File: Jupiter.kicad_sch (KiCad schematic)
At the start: 347 parts, among them SW1 SW_Push, U1 ATmega32U4-M, Y1 Crystal_GND24_Small

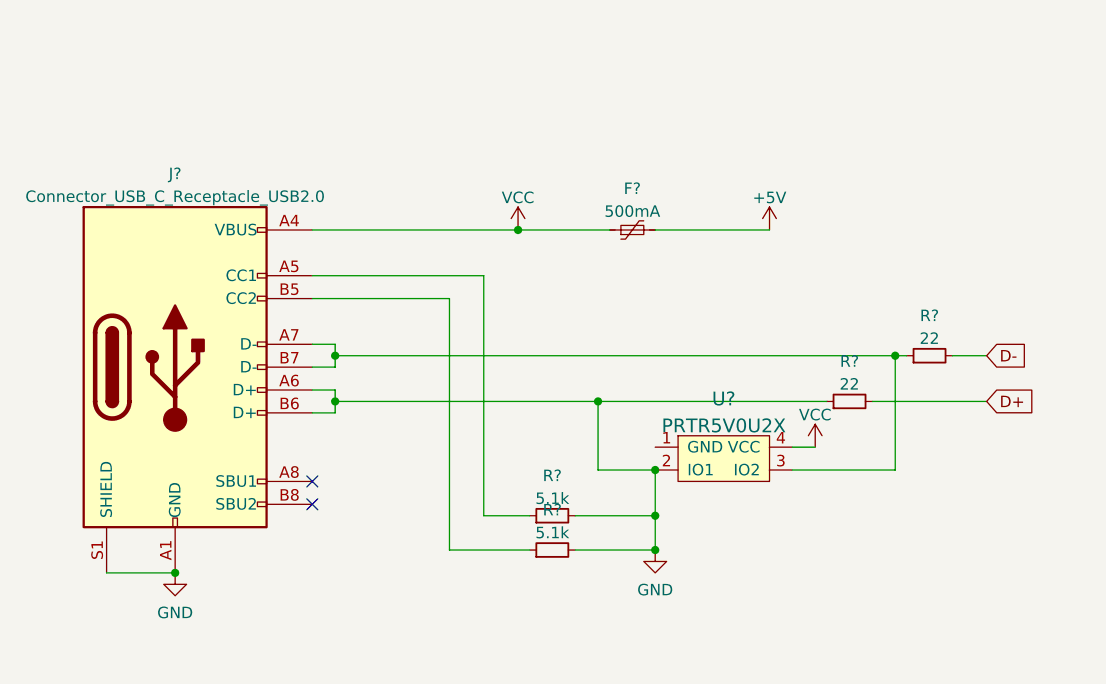
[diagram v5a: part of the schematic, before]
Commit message: Finished usb-c assembly
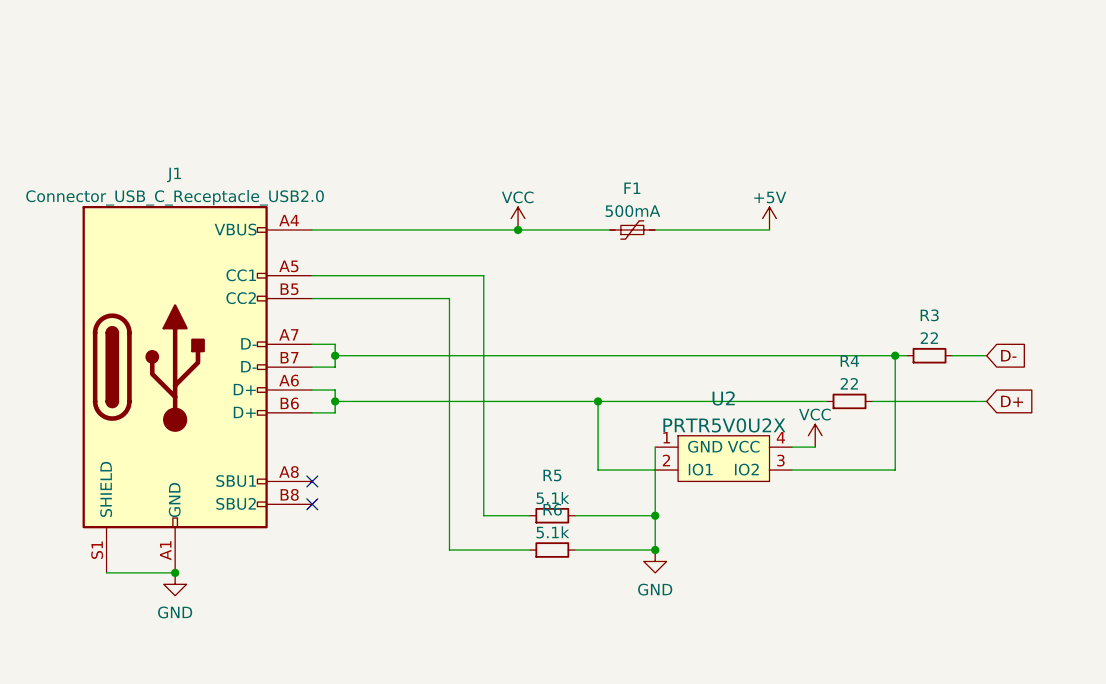
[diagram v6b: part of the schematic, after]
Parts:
- F1: renamed from F?; footprint (none) -> Fuse:Fuse_1206_3216Metric
- J1: renamed from J?; footprint (none) -> marbastlib-various:USB_C_Receptacle_HRO_TYPE-C-31-M-14
- R3, R4, R5, R6: renamed from R?; footprint (none) -> Resistor_SMD:R_0603_1608Metric
- U2: renamed from U?; footprint (none) -> random-keyboard-parts:SOT143B
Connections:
- net GND: now also U2.1 (GND); no longer J1.A6 (D+), J1.B6 (D+), R4.1, U2.2 (IO1)
- new net: J1.A6 (D+), J1.B6 (D+), R4.1, U2.2 (IO1)
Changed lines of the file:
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@@
   (junction (at 90.17 114.3) (diameter 0) (color 0 0 0 0)
   )
-  (junction (at 519.43 69.85) (diameter 0) (color 0 0 0 0)
-  )
   (junction (at 140.97 351.79) (diameter 0) (color 0 0 0 0)
   )
@@
   (junction (at 252.73 198.12) (diameter 0) (color 0 0 0 0)
   )
+  (junction (at 519.43 69.85) (diameter 0) (color 0 0 0 0)
+  )
   (junction (at 100.33 152.4) (diameter 0) (color 0 0 0 0)
   )
@@
   (junction (at 292.1 386.08) (diameter 0) (color 0 0 0 0)
   )
-  (junction (at 519.43 64.77) (diameter 0) (color 0 0 0 0)
-  )
   (junction (at 292.1 363.22) (diameter 0) (color 0 0 0 0)
   )
@@
     (stroke (width 0) (type default) (color 0 0 0 0))
   )
+  (wire (pts (xy 519.43 62.23) (xy 519.43 69.85))
+    (stroke (width 0) (type default) (color 0 0 0 0))
+  )
   (wire (pts (xy 313.69 242.57) (xy 344.17 242.57))
     (stroke (width 0) (type default) (color 0 0 0 0))
@@
     (stroke (width 0) (type default) (color 0 0 0 0))
   )
-  (wire (pts (xy 519.43 64.77) (xy 519.43 69.85))
-    (stroke (width 0) (type default) (color 0 0 0 0))
-  )
   (wire (pts (xy 223.52 95.25) (xy 240.03 95.25))
     (stroke (width 0) (type default) (color 0 0 0 0))
@@
   (symbol (lib_id "power:GND") (at 466.09 76.2 0) (unit 1)
     (in_bom yes) (on_board yes) (fields_autoplaced)
-    (property "Reference" "#PWR?" (id 0) (at 466.09 82.55 0)
+    (property "Reference" "#PWR0109" (id 0) (at 466.09 82.55 0)
       (effects (font (size 1.27 1.27)) hide)
     )
@@
   (symbol (lib_id "power:+5V") (at 532.13 38.1 0) (unit 1)
     (in_bom yes) (on_board yes) (fields_autoplaced)
-    (property "Reference" "#PWR?" (id 0) (at 532.13 41.91 0)
+    (property "Reference" "#PWR0110" (id 0) (at 532.13 41.91 0)
       (effects (font (size 1.27 1.27)) hide)
     )
@@
   (symbol (lib_id "power:VCC") (at 504.19 38.1 0) (unit 1)
     (in_bom yes) (on_board yes) (fields_autoplaced)
-    (property "Reference" "#PWR?" (id 0) (at 504.19 41.91 0)
+    (property "Reference" "#PWR0118" (id 0) (at 504.19 41.91 0)
       (effects (font (size 1.27 1.27)) hide)
     )
@@
   (symbol (lib_id "USB-C-USB-2.0-cache:Connector_USB_C_Receptacle_USB2.0") (at 466.09 53.34 0) (unit 1)
     (in_bom yes) (on_board yes) (fields_autoplaced)
-    (property "Reference" "J?" (id 0) (at 466.09 31.8602 0))
+    (property "Reference" "J1" (id 0) (at 466.09 31.8602 0))
     (property "Value" "Connector_USB_C_Receptacle_USB2.0" (id 1) (at 466.09 34.3971 0))
-    (property "Footprint" "" (id 2) (at 469.9 53.34 0)
+    (property "Footprint" "marbastlib-various:USB_C_Receptacle_HRO_TYPE-C-31-M-14" (id 2) (at 469.9 53.34 0)
       (effects (font (size 1.27 1.27)) hide)
     )
@@
   (symbol (lib_id "random-keyboard-parts:PRTR5V0U2X") (at 527.05 63.5 0) (unit 1)
     (in_bom yes) (on_board yes) (fields_autoplaced)
-    (property "Reference" "U?" (id 0) (at 527.05 56.8759 0)
+    (property "Reference" "U2" (id 0) (at 527.05 56.8759 0)
       (effects (font (size 1.524 1.524)))
     )
@@
       (effects (font (size 1.524 1.524)))
     )
-    (property "Footprint" "" (id 2) (at 527.05 63.5 0)
+    (property "Footprint" "random-keyboard-parts:SOT143B" (id 2) (at 527.05 63.5 0)
       (effects (font (size 1.524 1.524)) hide)
     )
@@
   (symbol (lib_id "power:VCC") (at 537.21 62.23 0) (unit 1)
     (in_bom yes) (on_board yes) (fields_autoplaced)
-    (property "Reference" "#PWR?" (id 0) (at 537.21 66.04 0)
+    (property "Reference" "#PWR0117" (id 0) (at 537.21 66.04 0)
       (effects (font (size 1.27 1.27)) hide)
     )
@@
   (symbol (lib_id "Device:R_Small") (at 508 69.85 90) (unit 1)
     (in_bom yes) (on_board yes) (fields_autoplaced)
-    (property "Reference" "R?" (id 0) (at 508 65.4136 90))
+    (property "Reference" "R5" (id 0) (at 508 65.4136 90))
     (property "Value" "5.1k" (id 1) (at 508 67.9505 90))
-    (property "Footprint" "" (id 2) (at 508 69.85 0)
+    (property "Footprint" "Resistor_SMD:R_0603_1608Metric" (id 2) (at 508 69.85 0)
       (effects (font (size 1.27 1.27)) hide)
     )
@@
   (symbol (lib_id "Device:R_Small") (at 508 73.66 90) (unit 1)
     (in_bom yes) (on_board yes) (fields_autoplaced)
-    (property "Reference" "R?" (id 0) (at 508 69.2236 90))
+    (property "Reference" "R6" (id 0) (at 508 69.2236 90))
     (property "Value" "5.1k" (id 1) (at 508 71.7605 90))
-    (property "Footprint" "" (id 2) (at 508 73.66 0)
+    (property "Footprint" "Resistor_SMD:R_0603_1608Metric" (id 2) (at 508 73.66 0)
       (effects (font (size 1.27 1.27)) hide)
     )
@@
   (symbol (lib_id "Device:R_Small") (at 541.02 57.15 90) (unit 1)
     (in_bom yes) (on_board yes) (fields_autoplaced)
-    (property "Reference" "R?" (id 0) (at 541.02 52.7136 90))
+    (property "Reference" "R4" (id 0) (at 541.02 52.7136 90))
     (property "Value" "22" (id 1) (at 541.02 55.2505 90))
-    (property "Footprint" "" (id 2) (at 541.02 57.15 0)
+    (property "Footprint" "Resistor_SMD:R_0603_1608Metric" (id 2) (at 541.02 57.15 0)
       (effects (font (size 1.27 1.27)) hide)
     )
@@
   (symbol (lib_id "Device:Polyfuse_Small") (at 516.89 38.1 90) (unit 1)
     (in_bom yes) (on_board yes) (fields_autoplaced)
-    (property "Reference" "F?" (id 0) (at 516.89 33.5112 90))
+    (property "Reference" "F1" (id 0) (at 516.89 33.5112 90))
     (property "Value" "500mA" (id 1) (at 516.89 36.0481 90))
-    (property "Footprint" "" (id 2) (at 521.97 36.83 0)
+    (property "Footprint" "Fuse:Fuse_1206_3216Metric" (id 2) (at 521.97 36.83 0)
       (effects (font (size 1.27 1.27)) (justify left) hide)
     )
@@
   (symbol (lib_id "Device:R_Small") (at 549.91 52.07 90) (unit 1)
     (in_bom yes) (on_board yes) (fields_autoplaced)
-    (property "Reference" "R?" (id 0) (at 549.91 47.6336 90))
+    (property "Reference" "R3" (id 0) (at 549.91 47.6336 90))
     (property "Value" "22" (id 1) (at 549.91 50.1705 90))
-    (property "Footprint" "" (id 2) (at 549.91 52.07 0)
+    (property "Footprint" "Resistor_SMD:R_0603_1608Metric" (id 2) (at 549.91 52.07 0)
       (effects (font (size 1.27 1.27)) hide)
     )
@@
   (symbol (lib_id "power:GND") (at 519.43 73.66 0) (unit 1)
     (in_bom yes) (on_board yes) (fields_autoplaced)
-    (property "Reference" "#PWR?" (id 0) (at 519.43 80.01 0)
+    (property "Reference" "#PWR0119" (id 0) (at 519.43 80.01 0)
       (effects (font (size 1.27 1.27)) hide)
     )
@@
       (reference "#PWR0108") (unit 1) (value "+5V") (footprint "")
     )
+    (path "/1a853bec-a5b0-4182-9ebb-c3db3d497370"
+      (reference "#PWR0109") (unit 1) (value "GND") (footprint "")
+    )
+    (path "/29f4c1eb-6384-43cf-a1dc-29fc79670556"
+      (reference "#PWR0110") (unit 1) (value "+5V") (footprint "")
+    )
     (path "/3343379b-1d26-41c6-8015-955e176890b7"
       (reference "#PWR0111") (unit 1) (value "GND") (footprint "")
@@
       (reference "#PWR0116") (unit 1) (value "GND") (footprint "")
     )
-    (path "/1a853bec-a5b0-4182-9ebb-c3db3d497370"
-      (reference "#PWR?") (unit 1) (value "GND") (footprint "")
-    )
-    (path "/29f4c1eb-6384-43cf-a1dc-29fc79670556"
-      (reference "#PWR?") (unit 1) (value "+5V") (footprint "")
+    (path "/7e537112-97b3-461a-9476-143d1b62889d"
+      (reference "#PWR0117") (unit 1) (value "VCC") (footprint "")
     )
     (path "/420034f2-5c0b-42e1-bffd-0fdb40e4bbe6"
-      (reference "#PWR?") (unit 1) (value "VCC") (footprint "")
-    )
-    (path "/7e537112-97b3-461a-9476-143d1b62889d"
-      (reference "#PWR?") (unit 1) (value "VCC") (footprint "")
+      (reference "#PWR0118") (unit 1) (value "VCC") (footprint "")
     )
     (path "/fe6eeca3-df26-4a38-ad33-9eb31c26b9b9"
-      (reference "#PWR?") (unit 1) (value "GND") (footprint "")
+      (reference "#PWR0119") (unit 1) (value "GND") (footprint "")
     )
     (path "/213d1ae6-3493-4a17-9c56-b781ec3d5fab"
@@
     )
     (path "/c16d0013-4ad3-4974-b494-e8139c1e7f2b"
-      (reference "F?") (unit 1) (value "500mA") (footprint "")
+      (reference "F1") (unit 1) (value "500mA") (footprint "Fuse:Fuse_1206_3216Metric")
     )
     (path "/59ae39a2-cb9c-4d24-8c9e-792b7b0ffd9c"
-      (reference "J?") (unit 1) (value "Connector_USB_C_Receptacle_USB2.0") (footprint "")
+      (reference "J1") (unit 1) (value "Connector_USB_C_Receptacle_USB2.0") (footprint "marbastlib-various:USB_C_Receptacle_HRO_TYPE-C-31-M-14")
     )
     (path "/9de686b4-dca8-4f88-a6cb-b8703cee154a"
@@
       (reference "R2") (unit 1) (value "1k") (footprint "Resistor_SMD:R_0603_1608Metric")
     )
-    (path "/a262535b-6894-4840-8bc5-64fe50cf0d6a"
-      (reference "R?") (unit 1) (value "5.1k") (footprint "")
-    )
-    (path "/b245d22d-2850-402a-ad41-44b03576cca4"
-      (reference "R?") (unit 1) (value "5.1k") (footprint "")
+    (path "/f6530bbb-3235-446b-90bd-62bba5916f8f"
+      (reference "R3") (unit 1) (value "22") (footprint "Resistor_SMD:R_0603_1608Metric")
     )
     (path "/c0d15e4a-ba5d-4176-87b9-5561f2edf504"
-      (reference "R?") (unit 1) (value "22") (footprint "")
+      (reference "R4") (unit 1) (value "22") (footprint "Resistor_SMD:R_0603_1608Metric")
     )
-    (path "/f6530bbb-3235-446b-90bd-62bba5916f8f"
-      (reference "R?") (unit 1) (value "22") (footprint "")
+    (path "/a262535b-6894-4840-8bc5-64fe50cf0d6a"
+      (reference "R5") (unit 1) (value "5.1k") (footprint "Resistor_SMD:R_0603_1608Metric")
+    )
+    (path "/b245d22d-2850-402a-ad41-44b03576cca4"
+      (reference "R6") (unit 1) (value "5.1k") (footprint "Resistor_SMD:R_0603_1608Metric")
     )
     (path "/20226c85-96ea-44d3-a255-4e1300fb3be7"
@@
     )
     (path "/5e25d345-8130-4e41-bd8d-fd468aef5828"
-      (reference "U?") (unit 1) (value "PRTR5V0U2X") (footprint "")
+      (reference "U2") (unit 1) (value "PRTR5V0U2X") (footprint "random-keyboard-parts:SOT143B")
     )
     (path "/1da16e64-cd89-47c6-a15d-a5d97941d7ac"

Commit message: Corrected LED orientation
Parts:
- LED_0, LED_1, LED_2, LED_3, LED_4, LED_5, LED_6, LED_7, LED_8, LED_9, LED_A1, LED_D1, LED_F13, LED_G1, LED_H1, LED_J1, LED_K1, LED_L1, LED_S1, LED_backspace1, LED_capsLock1, LED_colon1, LED_downArrow1, LED_end1, LED_enter1, LED_equals1, LED_function1, LED_leftAlt1, LED_leftArrow1, LED_leftControl1, LED_minus1, LED_pgDn1, LED_pgUp1, LED_quote1, LED_rightAlt1, LED_rightArrow1, LED_rightControl1, LED_space1, LED_tilda1, LED_windows1: footprint marbastlib-mx:LED_MX_6028R-FLIPPED -> marbastlib-mx:LED_MX_6028R
- LED_B1, LED_C1, LED_E1, LED_F1, LED_F10, LED_F11, LED_F12, LED_F2, LED_F3, LED_F4, LED_F5, LED_F6, LED_F7, LED_F8, LED_F9, LED_I1, LED_M1, LED_N1, LED_O1, LED_P1, LED_Q1, LED_R1, LED_T1, LED_U1, LED_V1, LED_W1, LED_X1, LED_Y1, LED_Z1, LED_backslash1, LED_closeBracket1, LED_comma1, LED_delete1, LED_esc1, LED_home1, LED_leftShift1, LED_openBracket1, LED_period1, LED_questionMark1, LED_rightShift1, LED_tab1, LED_upArrow1: footprint marbastlib-mx:LED_MX_6028R -> marbastlib-mx:LED_MX_6028R-FLIPPED
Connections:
- net COL14: now also U1.10 (PB2); no longer U1.9 (PB1)
- net GND: now also J1.A6 (D+), J1.B6 (D+), R4.1, U2.2 (IO1); no longer U2.1 (GND)
- net RGBLED: now also LED_home1.3 (DIN), U1.9 (PB1); no longer LED_end1.3 (DIN), U1.12 (PB7)
- net ROW4: now also U1.11 (PB3); no longer U1.10 (PB2)
- net ROW5: now also U1.12 (PB7); no longer U1.11 (PB3)
- net at LED_Q1.2 (DOUT): now also LED_W1.3 (DIN); no longer LED_tab1.3 (DIN)
- net at LED_Q1.3 (DIN): now also LED_tab1.2 (DOUT); no longer LED_W1.2 (DOUT)
- net at LED_upArrow1.2 (DOUT): now also LED_enter1.3 (DIN); no longer LED_rightShift1.3 (DIN)
- net at LED_upArrow1.3 (DIN): now also LED_rightShift1.2 (DOUT); no longer LED_enter1.2 (DOUT)
- net at LED_F2.2 (DOUT): now also LED_F3.3 (DIN); no longer LED_F1.3 (DIN)
- net at LED_F2.3 (DIN): now also LED_F1.2 (DOUT); no longer LED_F3.2 (DOUT)
- net at LED_leftControl1.2 (DOUT): now also LED_leftShift1.3 (DIN); no longer LED_windows1.3 (DIN)
- net at LED_leftControl1.3 (DIN): now also LED_windows1.2 (DOUT); no longer LED_leftShift1.2 (DOUT)
- net at LED_K1.2 (DOUT): now also LED_J1.3 (DIN); no longer LED_L1.3 (DIN)
- net at LED_K1.3 (DIN): now also LED_L1.2 (DOUT); no longer LED_J1.2 (DOUT)
- net at LED_leftArrow1.2 (DOUT): now also LED_rightControl1.3 (DIN); no longer LED_downArrow1.3 (DIN)
- net at LED_leftArrow1.3 (DIN): now also LED_downArrow1.2 (DOUT); no longer LED_rightControl1.2 (DOUT)
- net at LED_colon1.3 (DIN): now also LED_quote1.2 (DOUT); no longer LED_L1.2 (DOUT)
- net at LED_F6.2 (DOUT): now also LED_F7.3 (DIN); no longer LED_F5.3 (DIN)
- net at LED_F6.3 (DIN): now also LED_F5.2 (DOUT); no longer LED_F7.2 (DOUT)
- net at LED_questionMark1.2 (DOUT): now also LED_rightShift1.3 (DIN); no longer LED_period1.3 (DIN)
- net at LED_questionMark1.3 (DIN): now also LED_period1.2 (DOUT); no longer LED_rightShift1.2 (DOUT)
- net at LED_4.2 (DOUT): now also LED_3.3 (DIN); no longer LED_5.3 (DIN)
- net at LED_4.3 (DIN): now also LED_5.2 (DOUT); no longer LED_3.2 (DOUT)
- net at LED_Z1.2 (DOUT): now also LED_X1.3 (DIN); no longer LED_leftShift1.3 (DIN)
- net at LED_minus1.2 (DOUT): now also LED_0.3 (DIN); no longer LED_equals1.3 (DIN)
- net at LED_minus1.3 (DIN): now also LED_equals1.2 (DOUT); no longer LED_0.2 (DOUT)
- net at LED_leftAlt1.3 (DIN): now also LED_space1.2 (DOUT); no longer LED_windows1.2 (DOUT)
- net at LED_9.2 (DOUT): now also LED_8.3 (DIN); no longer LED_0.3 (DIN)
- net at LED_9.3 (DIN): now also LED_0.2 (DOUT); no longer LED_8.2 (DOUT)
- net at LED_S1.2 (DOUT): now also LED_A1.3 (DIN); no longer LED_D1.3 (DIN)
- net at LED_S1.3 (DIN): now also LED_D1.2 (DOUT); no longer LED_A1.2 (DOUT)
- net at LED_esc1.3 (DIN): now also LED_tilda1.2 (DOUT); no longer LED_F1.2 (DOUT)
- net at LED_rightArrow1.2 (DOUT): now also LED_downArrow1.3 (DIN)
- net at LED_rightArrow1.3 (DIN): now also LED_end1.2 (DOUT); no longer LED_downArrow1.2 (DOUT)
- net at LED_F8.2 (DOUT): now also LED_F9.3 (DIN); no longer LED_F7.3 (DIN)
- net at LED_F4.2 (DOUT): now also LED_F5.3 (DIN); no longer LED_F3.3 (DIN)
- net at LED_C1.2 (DOUT): now also LED_V1.3 (DIN); no longer LED_X1.3 (DIN)
- net at LED_C1.3 (DIN): now also LED_X1.2 (DOUT); no longer LED_V1.2 (DOUT)
- net at LED_backspace1.2 (DOUT): now also LED_equals1.3 (DIN); no longer LED_backslash1.3 (DIN)
- net at LED_backspace1.3 (DIN): now also LED_backslash1.2 (DOUT); no longer LED_equals1.2 (DOUT)
- net at LED_F4.3 (DIN): now also LED_F3.2 (DOUT); no longer LED_F5.2 (DOUT)
- net at LED_Y1.2 (DOUT): now also LED_U1.3 (DIN); no longer LED_T1.3 (DIN)
- net at LED_Y1.3 (DIN): now also LED_T1.2 (DOUT); no longer LED_U1.2 (DOUT)
- net at LED_function1.2 (DOUT): now also LED_rightAlt1.3 (DIN); no longer LED_rightControl1.3 (DIN)
- net at LED_function1.3 (DIN): now also LED_rightControl1.2 (DOUT); no longer LED_rightAlt1.2 (DOUT)
- net at LED_pgUp1.2 (DOUT): now also LED_pgDn1.3 (DIN); no longer LED_home1.3 (DIN)
- net at LED_pgUp1.3 (DIN): now also LED_home1.2 (DOUT); no longer LED_pgDn1.2 (DOUT)
- net at LED_M1.2 (DOUT): now also LED_comma1.3 (DIN); no longer LED_N1.3 (DIN)
- net at LED_M1.3 (DIN): now also LED_N1.2 (DOUT); no longer LED_comma1.2 (DOUT)
- net at LED_delete1.2 (DOUT): no longer LED_F12.3 (DIN)
- net at LED_delete1.3 (DIN): now also LED_F12.2 (DOUT); no longer LED_home1.2 (DOUT)
- net at LED_R1.2 (DOUT): now also LED_T1.3 (DIN); no longer LED_E1.3 (DIN)
- net at LED_R1.3 (DIN): now also LED_E1.2 (DOUT); no longer LED_T1.2 (DOUT)
- net at LED_Z1.3 (DIN): now also LED_leftShift1.2 (DOUT); no longer LED_X1.2 (DOUT)
- net at LED_F8.3 (DIN): now also LED_F7.2 (DOUT); no longer LED_F9.2 (DOUT)
- net at LED_2.2 (DOUT): now also LED_1.3 (DIN); no longer LED_3.3 (DIN)
- net at LED_2.3 (DIN): now also LED_3.2 (DOUT); no longer LED_1.2 (DOUT)
- net at LED_leftAlt1.2 (DOUT): now also LED_windows1.3 (DIN); no longer LED_space1.3 (DIN)
- net at LED_F11.2 (DOUT): now also LED_F12.3 (DIN); no longer LED_F10.3 (DIN)
- net at LED_F11.3 (DIN): now also LED_F10.2 (DOUT); no longer LED_F12.2 (DOUT)
- net at LED_colon1.2 (DOUT): now also LED_L1.3 (DIN); no longer LED_quote1.3 (DIN)
- net at LED_capsLock1.2 (DOUT): now also LED_tab1.3 (DIN); no longer LED_A1.3 (DIN)
- net at LED_7.2 (DOUT): now also LED_6.3 (DIN); no longer LED_8.3 (DIN)
- net at LED_7.3 (DIN): now also LED_8.2 (DOUT); no longer LED_6.2 (DOUT)
- net at LED_esc1.2 (DOUT): now also LED_F1.3 (DIN); no longer LED_tilda1.3 (DIN)
- net at LED_capsLock1.3 (DIN): now also LED_A1.2 (DOUT); no longer LED_tab1.2 (DOUT)
- net at LED_closeBracket1.3 (DIN): now also LED_openBracket1.2 (DOUT); no longer LED_backslash1.2 (DOUT)
- net at LED_B1.2 (DOUT): now also LED_N1.3 (DIN); no longer LED_V1.3 (DIN)
- net at LED_G1.2 (DOUT): now also LED_F13.3 (DIN); no longer LED_H1.3 (DIN)
- net at LED_G1.3 (DIN): now also LED_H1.2 (DOUT); no longer LED_F13.2 (DOUT)
- net at LED_closeBracket1.2 (DOUT): now also LED_backslash1.3 (DIN); no longer LED_openBracket1.3 (DIN)
- net at LED_B1.3 (DIN): now also LED_V1.2 (DOUT); no longer LED_N1.2 (DOUT)
- net at LED_P1.3 (DIN): now also LED_O1.2 (DOUT); no longer LED_openBracket1.2 (DOUT)
- net at LED_P1.2 (DOUT): now also LED_openBracket1.3 (DIN); no longer LED_O1.3 (DIN)
- net at LED_I1.2 (DOUT): now also LED_O1.3 (DIN); no longer LED_U1.3 (DIN)
- net at LED_I1.3 (DIN): now also LED_U1.2 (DOUT); no longer LED_O1.2 (DOUT)
- new net: LED_E1.3 (DIN), LED_W1.2 (DOUT)
- new net: LED_end1.3 (DIN), LED_pgDn1.2 (DOUT)
- new net: LED_comma1.2 (DOUT), LED_period1.3 (DIN)
- new net: LED_enter1.2 (DOUT), LED_quote1.3 (DIN)
- new net: LED_F10.3 (DIN), LED_F9.2 (DOUT)
- new net: LED_1.2 (DOUT), LED_tilda1.3 (DIN)
- new net: LED_5.3 (DIN), LED_6.2 (DOUT)
- new net: LED_rightAlt1.2 (DOUT), LED_space1.3 (DIN)
- new net: LED_D1.3 (DIN), LED_F13.2 (DOUT)
- new net: LED_H1.3 (DIN), LED_J1.2 (DOUT)
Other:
- moved on the sheet: C1, C10, C11, C12, C13, C14, C15, C16, C17, C18, C19, C2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

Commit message: Finished trace routing
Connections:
- net GND: now also U2.1 (GND); no longer J1.A6 (D+), J1.B6 (D+), R4.1, U2.2 (IO1)
- new net: J1.A6 (D+), J1.B6 (D+), R4.1, U2.2 (IO1)
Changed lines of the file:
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@@
   (junction (at 332.74 265.43) (diameter 0) (color 0 0 0 0)
-  )
-  (junction (at 317.5 381) (diameter 0) (color 0 0 0 0)
   )
   (junction (at 472.44 242.57) (diameter 0) (color 0 0 0 0)
@@
     (stroke (width 0) (type default) (color 0 0 0 0))
   )
-  (wire (pts (xy 317.5 381) (xy 317.5 386.08))
-    (stroke (width 0) (type default) (color 0 0 0 0))
-  )
+  (wire (pts (xy 317.5 378.46) (xy 317.5 386.08))
+    (stroke (width 0) (type default) (color 0 0 0 0))
+  )
